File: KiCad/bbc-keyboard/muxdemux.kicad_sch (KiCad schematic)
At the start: 1 part, among them IC1 74LS161

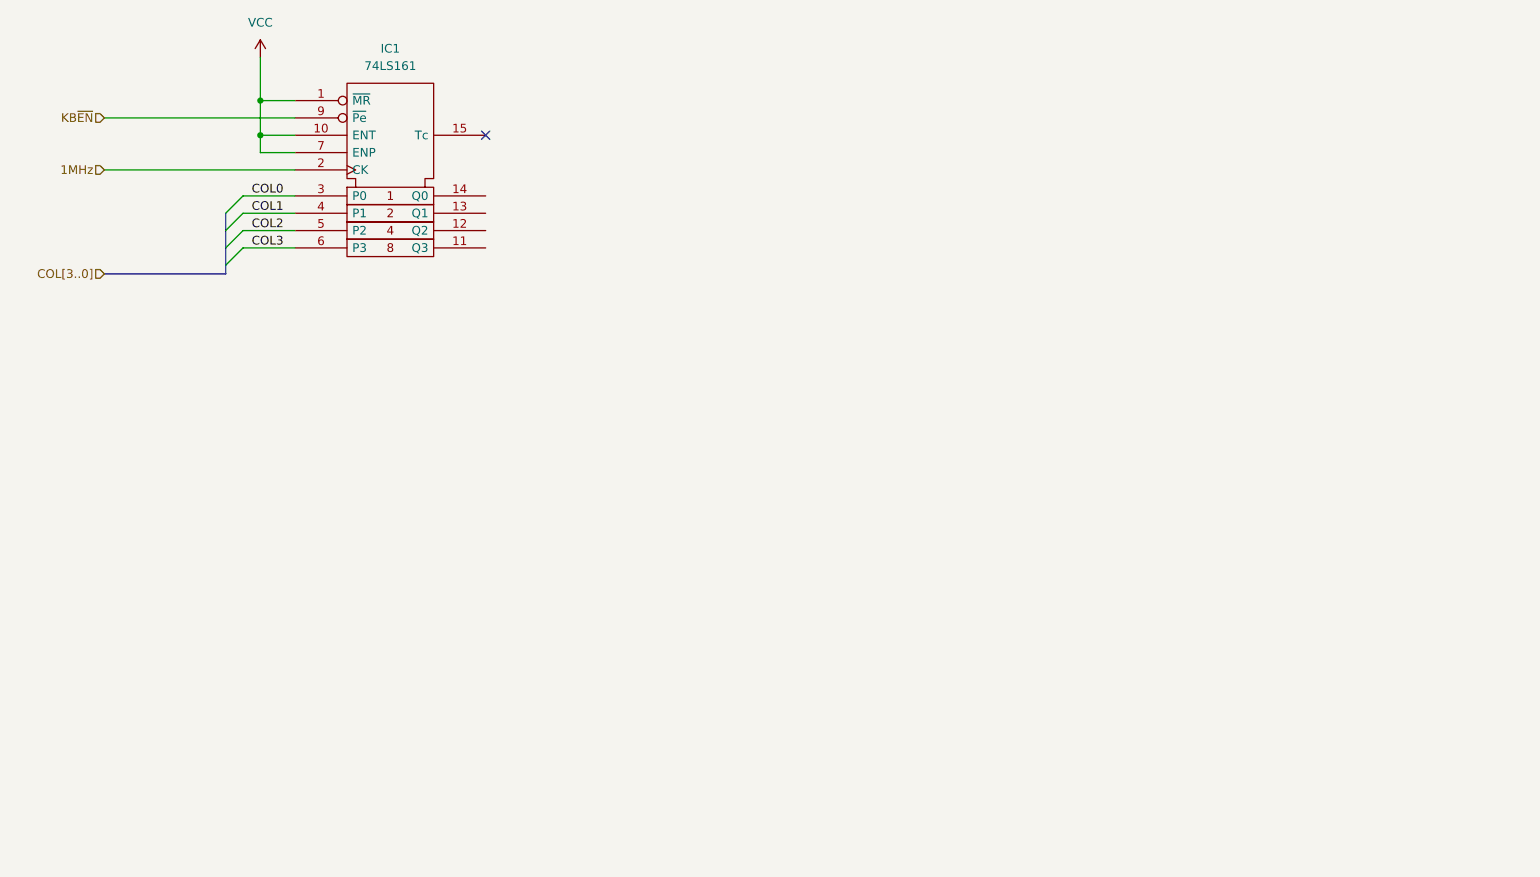
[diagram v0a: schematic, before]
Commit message: 1st cut mux/demux
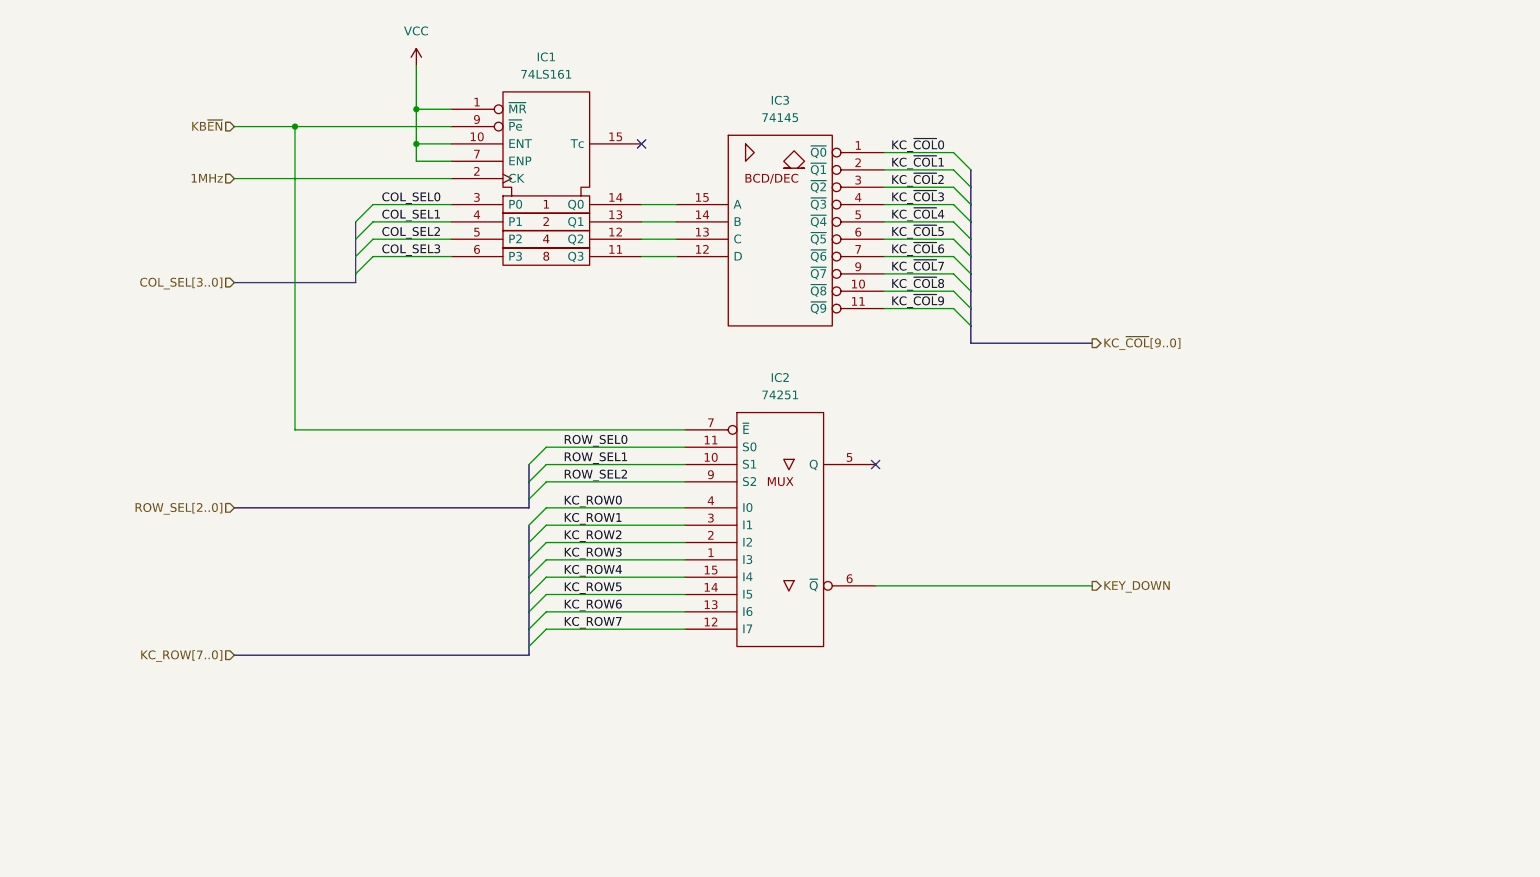
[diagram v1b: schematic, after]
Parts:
- added IC2: 74251, symbol 74xx_IEEE:74251
- added IC3: 74145, symbol 74xx_IEEE:74145
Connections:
- net GND: now also IC2.8 (GND), IC3.8 (GND)
- net KB~{EN}: now also IC2.7 (~{E})
- net VCC: now also IC2.16 (VCC), IC3.16 (VCC)
- net at IC1.11 (Q3): now also IC3.12 (D)
- net at IC1.12 (Q2): now also IC3.13 (C)
- net at IC1.13 (Q1): now also IC3.14 (B)
- net at IC1.14 (Q0): now also IC3.15 (A)
- net COL0 renamed COL_SEL0
- net COL1 renamed COL_SEL1
- net COL2 renamed COL_SEL2
- net COL3 renamed COL_SEL3
- new net KC_ROW0: IC2.4 (I0)
- new net KC_ROW1: IC2.3 (I1)
- new net KC_ROW2: IC2.2 (I2)
- new net KC_ROW3: IC2.1 (I3)
- new net KC_ROW4: IC2.15 (I4)
- new net KC_ROW5: IC2.14 (I5)
- new net KC_ROW6: IC2.13 (I6)
- new net KC_ROW7: IC2.12 (I7)
- new net KC_~{COL}0: IC3.1 (~{Q0})
- new net KC_~{COL}1: IC3.2 (~{Q1})
- new net KC_~{COL}2: IC3.3 (~{Q2})
- new net KC_~{COL}3: IC3.4 (~{Q3})
- new net KC_~{COL}4: IC3.5 (~{Q4})
- new net KC_~{COL}5: IC3.6 (~{Q5})
- new net KC_~{COL}6: IC3.7 (~{Q6})
- new net KC_~{COL}7: IC3.9 (~{Q7})
- new net KC_~{COL}8: IC3.10 (~{Q8})
- new net KC_~{COL}9: IC3.11 (~{Q9})
- new net KEY_DOWN: IC2.6 (~{Q})
- new net ROW_SEL0: IC2.11 (S0)
- new net ROW_SEL1: IC2.10 (S1)
- new net ROW_SEL2: IC2.9 (S2)
- no-connect marks 1 -> 2
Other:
- moved on the sheet: IC1

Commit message: muxdemux irq det
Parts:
- added IC4: 7430, symbol 74xx_IEEE:7430
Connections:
- net KC_ROW1: now also IC4.12
- net KC_ROW2: now also IC4.1
- net KC_ROW3: now also IC4.2
- net KC_ROW4: now also IC4.3
- net KC_ROW5: now also IC4.4
- net KC_ROW6: now also IC4.5
- net KC_ROW7: now also IC4.11
- net VCC: now also IC4.6
- new net Gnd: IC4.7 (Gnd)
- new net KEY_~{IRQ}: IC4.8
- new net Vcc: IC4.14 (Vcc)

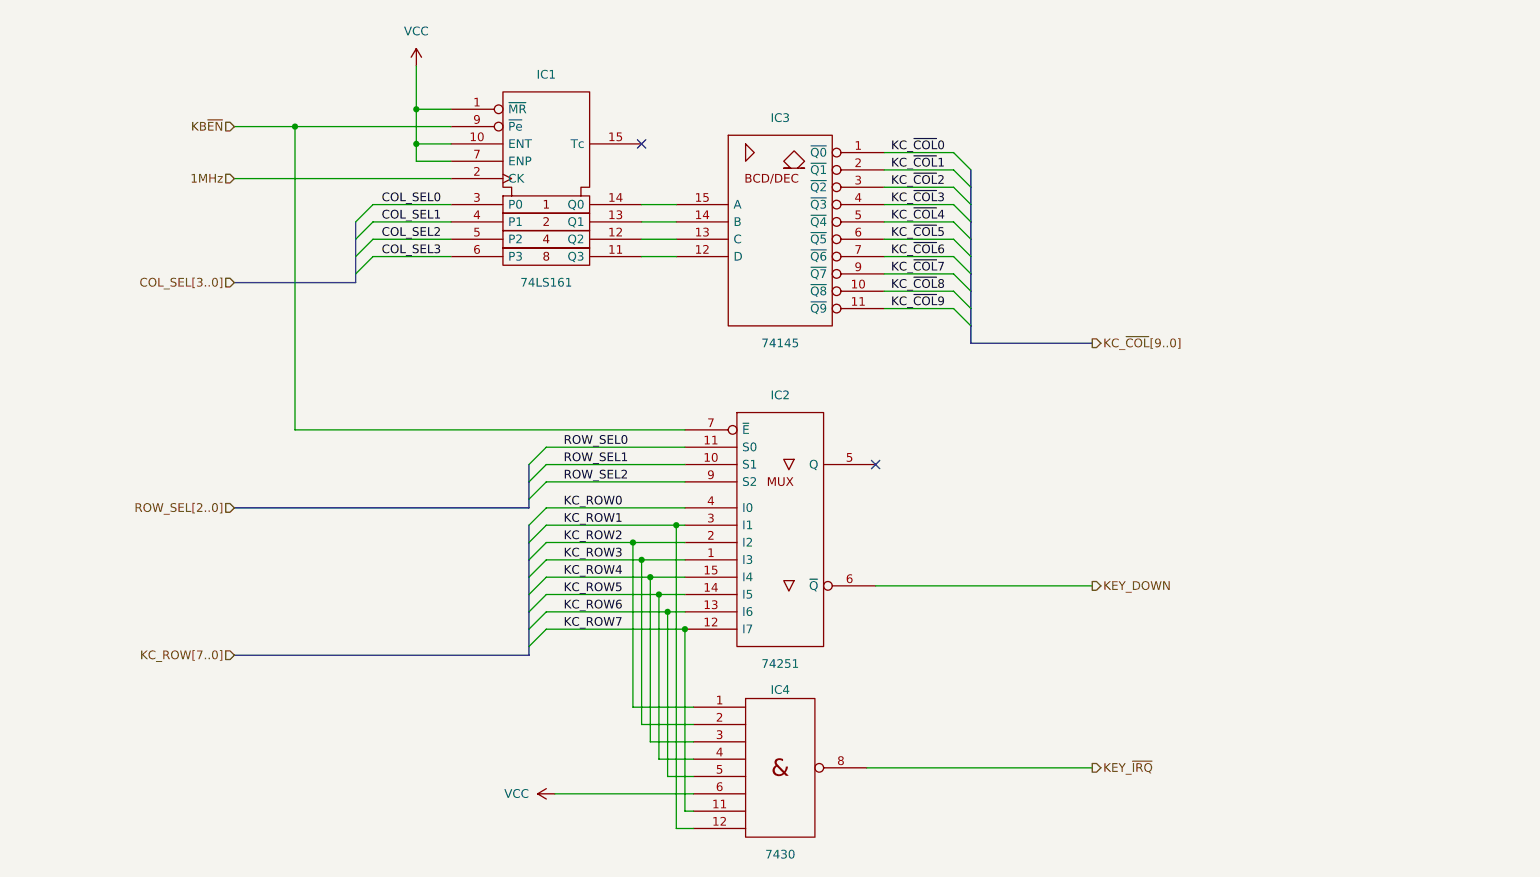
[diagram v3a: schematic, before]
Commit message: pull ups
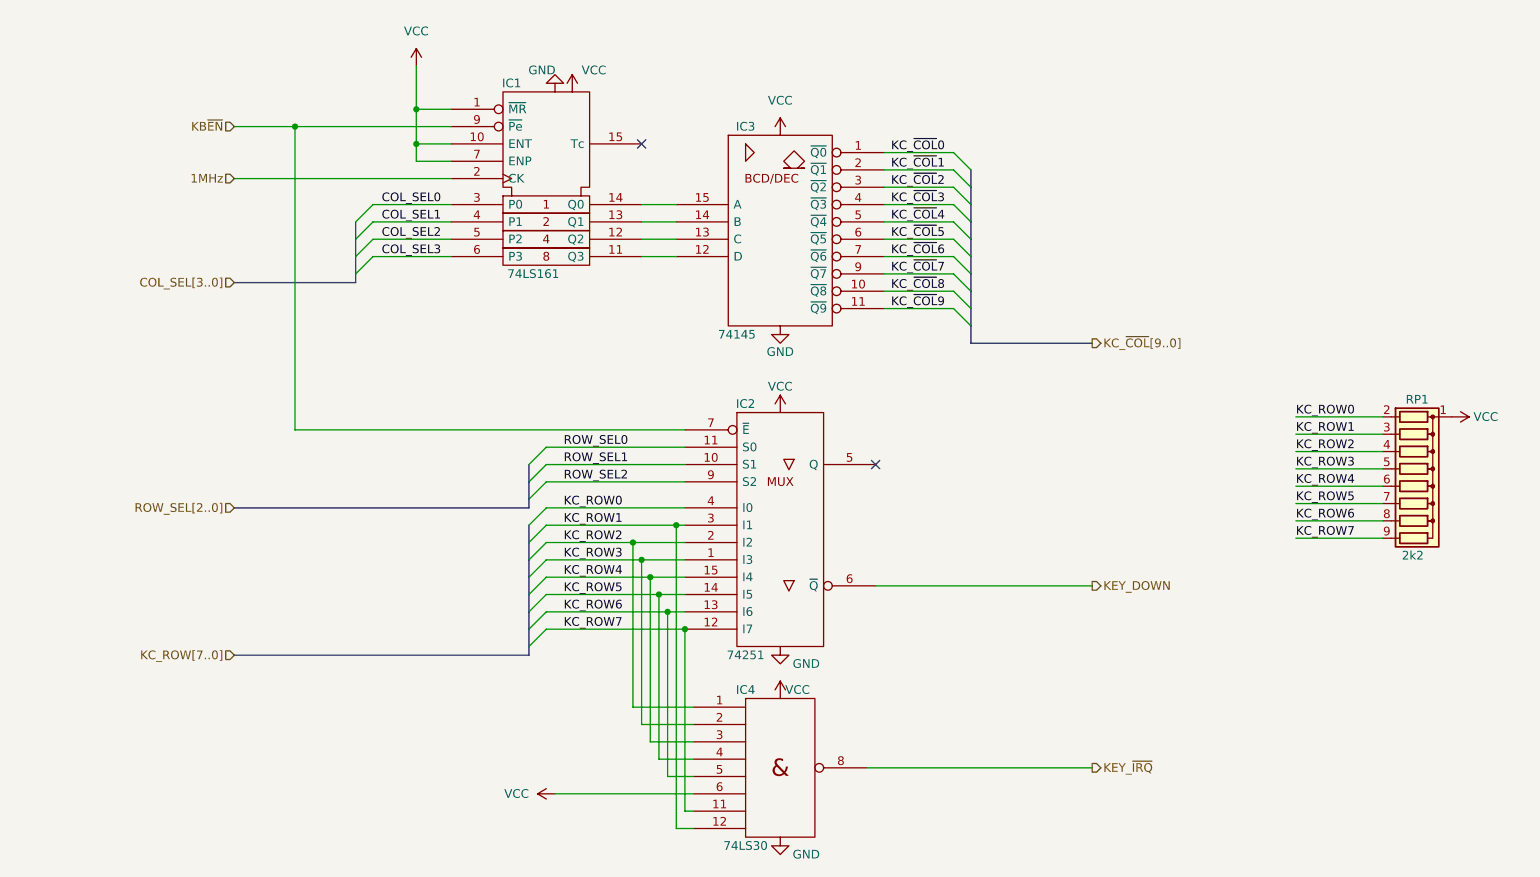
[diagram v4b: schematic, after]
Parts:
- added RP1: 2k2, Resistor_THT:R_Array_SIP9, symbol Device:R_Network08
- IC4: value 7430 -> 74LS30
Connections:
- net Gnd is gone; now on net GND: IC4.7 (Gnd)
- net Vcc is gone; now on net VCC: IC4.14 (Vcc)
- net KC_ROW0: now also RP1.2 (R1)
- net KC_ROW1: now also RP1.3 (R2)
- net KC_ROW2: now also RP1.4 (R3)
- net KC_ROW3: now also RP1.5 (R4)
- net KC_ROW4: now also RP1.6 (R5)
- net KC_ROW5: now also RP1.7 (R6)
- net KC_ROW6: now also RP1.8 (R7)
- net KC_ROW7: now also RP1.9 (R8)
- net VCC: now also RP1.1 (common)

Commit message: placing components
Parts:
- IC1, IC2, IC3: footprint (none) -> Package_DIP:DIP-16_W7.62mm
- IC4: footprint (none) -> Package_DIP:DIP-14_W7.62mm
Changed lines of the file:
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@@
     (property "Reference" "IC3" (id 0) (at 127 46.99 0))
     (property "Value" "74145" (id 1) (at 125.73 77.47 0))
-    (property "Footprint" "" (id 2) (at 132.08 62.23 0)
+    (property "Footprint" "Package_DIP:DIP-16_W7.62mm" (id 2) (at 132.08 62.23 0)
       (effects (font (size 1.27 1.27)) hide)
     )
@@
     (property "Reference" "IC1" (id 0) (at 92.71 40.64 0))
     (property "Value" "74LS161" (id 1) (at 95.885 68.58 0))
-    (property "Footprint" "" (id 2) (at 97.79 55.88 0)
+    (property "Footprint" "Package_DIP:DIP-16_W7.62mm" (id 2) (at 97.79 55.88 0)
       (effects (font (size 1.27 1.27)) hide)
     )
@@
     (property "Reference" "IC2" (id 0) (at 127 87.63 0))
     (property "Value" "74251" (id 1) (at 127 124.46 0))
-    (property "Footprint" "" (id 2) (at 132.08 105.41 0)
+    (property "Footprint" "Package_DIP:DIP-16_W7.62mm" (id 2) (at 132.08 105.41 0)
       (effects (font (size 1.27 1.27)) hide)
     )
@@
     (property "Reference" "IC4" (id 0) (at 127 129.54 0))
     (property "Value" "74LS30" (id 1) (at 127 152.4 0))
-    (property "Footprint" "" (id 2) (at 132.08 140.97 0)
+    (property "Footprint" "Package_DIP:DIP-14_W7.62mm" (id 2) (at 132.08 140.97 0)
       (effects (font (size 1.27 1.27)) hide)
     )

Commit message: routed rhs
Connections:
- net KC_ROW1: now also RP1.8 (R7); no longer RP1.3 (R2)
- net KC_ROW2: now also RP1.7 (R6); no longer RP1.4 (R3)
- net KC_ROW3: now also RP1.6 (R5); no longer RP1.5 (R4)
- net KC_ROW4: now also RP1.5 (R4); no longer RP1.6 (R5)
- net KC_ROW5: now also RP1.4 (R3); no longer RP1.7 (R6)
- net KC_ROW6: now also RP1.3 (R2); no longer RP1.8 (R7)
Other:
- moved on the sheet: RP1
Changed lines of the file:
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@@
     (stroke (width 0) (type default) (color 0 0 0 0))
   )
-  (wire (pts (xy 207.645 89.535) (xy 220.345 89.535))
+  (wire (pts (xy 210.82 128.27) (xy 223.52 128.27))
     (stroke (width 0) (type default) (color 0 0 0 0))
   )
@@
     (stroke (width 0) (type default) (color 0 0 0 0))
   )
-  (wire (pts (xy 207.645 107.315) (xy 220.345 107.315))
+  (wire (pts (xy 210.82 146.05) (xy 223.52 146.05))
     (stroke (width 0) (type default) (color 0 0 0 0))
   )
@@
     (stroke (width 0) (type default) (color 0 0 0 0))
   )
-  (wire (pts (xy 207.645 97.155) (xy 220.345 97.155))
+  (wire (pts (xy 210.82 135.89) (xy 223.52 135.89))
     (stroke (width 0) (type default) (color 0 0 0 0))
   )
@@
     (stroke (width 0) (type default) (color 0 0 0 0))
   )
-  (wire (pts (xy 207.645 102.235) (xy 220.345 102.235))
+  (wire (pts (xy 210.82 140.97) (xy 223.52 140.97))
     (stroke (width 0) (type default) (color 0 0 0 0))
   )
@@
     (stroke (width 0) (type default) (color 0 0 0 0))
   )
-  (wire (pts (xy 207.645 92.075) (xy 220.345 92.075))
+  (wire (pts (xy 210.82 130.81) (xy 223.52 130.81))
     (stroke (width 0) (type default) (color 0 0 0 0))
   )
@@
     (stroke (width 0) (type default) (color 0 0 0 0))
   )
-  (wire (pts (xy 207.645 94.615) (xy 220.345 94.615))
+  (wire (pts (xy 210.82 133.35) (xy 223.52 133.35))
     (stroke (width 0) (type default) (color 0 0 0 0))
   )
@@
     (stroke (width 0) (type default) (color 0 0 0 0))
   )
-  (wire (pts (xy 207.645 104.775) (xy 220.345 104.775))
+  (wire (pts (xy 210.82 143.51) (xy 223.52 143.51))
     (stroke (width 0) (type default) (color 0 0 0 0))
   )
@@
     (stroke (width 0) (type default) (color 0 0 0 0))
   )
-  (wire (pts (xy 207.645 99.695) (xy 220.345 99.695))
+  (wire (pts (xy 210.82 138.43) (xy 223.52 138.43))
     (stroke (width 0) (type default) (color 0 0 0 0))
   )
@@
     (effects (font (size 1.27 1.27)) (justify right bottom))
   )
-  (label "KC_ROW6" (at 207.645 104.775 0)
+  (label "KC_ROW6" (at 210.82 130.81 0)
     (effects (font (size 1.27 1.27)) (justify left bottom))
   )
@@
     (effects (font (size 1.27 1.27)) (justify left bottom))
   )
-  (label "KC_ROW3" (at 207.645 97.155 0)
+  (label "KC_ROW3" (at 210.82 138.43 0)
     (effects (font (size 1.27 1.27)) (justify left bottom))
   )
@@
     (effects (font (size 1.27 1.27)) (justify left bottom))
   )
-  (label "KC_ROW0" (at 207.645 89.535 0)
+  (label "KC_ROW0" (at 210.82 128.27 0)
     (effects (font (size 1.27 1.27)) (justify left bottom))
   )
@@
     (effects (font (size 1.27 1.27)) (justify left bottom))
   )
-  (label "KC_ROW1" (at 207.645 92.075 0)
+  (label "KC_ROW1" (at 210.82 143.51 0)
     (effects (font (size 1.27 1.27)) (justify left bottom))
   )
@@
     (effects (font (size 1.27 1.27)) (justify right bottom))
   )
-  (label "KC_ROW7" (at 207.645 107.315 0)
+  (label "KC_ROW7" (at 210.82 146.05 0)
     (effects (font (size 1.27 1.27)) (justify left bottom))
   )
@@
     (effects (font (size 1.27 1.27)) (justify right bottom))
   )
-  (label "KC_ROW4" (at 207.645 99.695 0)
+  (label "KC_ROW4" (at 210.82 135.89 0)
     (effects (font (size 1.27 1.27)) (justify left bottom))
   )
@@
     (effects (font (size 1.27 1.27)) (justify left bottom))
   )
-  (label "KC_ROW2" (at 207.645 94.615 0)
+  (label "KC_ROW2" (at 210.82 140.97 0)
     (effects (font (size 1.27 1.27)) (justify left bottom))
   )
@@
     (effects (font (size 1.27 1.27)) (justify left bottom))
   )
-  (label "KC_ROW5" (at 207.645 102.235 0)
+  (label "KC_ROW5" (at 210.82 133.35 0)
     (effects (font (size 1.27 1.27)) (justify left bottom))
   )
@@
     (pin "1")
   )
-  (symbol (lib_id "power:VCC") (at 230.505 89.535 270) (unit 1)
+  (symbol (lib_id "power:VCC") (at 233.68 128.27 270) (unit 1)
     (in_bom yes) (on_board yes) (fields_autoplaced)
-    (property "Reference" "#PWR0109" (id 0) (at 226.695 89.535 0)
-      (effects (font (size 1.27 1.27)) hide)
-    )
-    (property "Value" "VCC" (id 1) (at 233.68 89.5349 90)
+    (property "Reference" "#PWR0109" (id 0) (at 229.87 128.27 0)
+      (effects (font (size 1.27 1.27)) hide)
+    )
+    (property "Value" "VCC" (id 1) (at 236.855 128.2699 90)
       (effects (font (size 1.27 1.27)) (justify left))
     )
-    (property "Footprint" "" (id 2) (at 230.505 89.535 0)
-      (effects (font (size 1.27 1.27)) hide)
-    )
-    (property "Datasheet" "" (id 3) (at 230.505 89.535 0)
+    (property "Footprint" "" (id 2) (at 233.68 128.27 0)
+      (effects (font (size 1.27 1.27)) hide)
+    )
+    (property "Datasheet" "" (id 3) (at 233.68 128.27 0)
       (effects (font (size 1.27 1.27)) hide)
     )
@@
     (pin "1")
   )
-  (symbol (lib_id "Device:R_Network08") (at 225.425 99.695 270) (unit 1)
-    (in_bom yes) (on_board yes)
-    (property "Reference" "RP1" (id 0) (at 225.425 86.995 90))
-    (property "Value" "2k2" (id 1) (at 224.79 109.855 90))
-    (property "Footprint" "Resistor_THT:R_Array_SIP9" (id 2) (at 225.425 111.76 90)
-      (effects (font (size 1.27 1.27)) hide)
-    )
-    (property "Datasheet" "http://www.vishay.com/docs/31509/csc.pdf" (id 3) (at 225.425 99.695 0)
-      (effects (font (size 1.27 1.27)) hide)
-    )
+  (symbol (lib_id "Device:R_Network08") (at 228.6 138.43 270) (unit 1)
+    (in_bom yes) (on_board yes)
+    (property "Reference" "RP1" (id 0) (at 228.6 125.73 90))
+    (property "Value" "2k2" (id 1) (at 227.965 148.59 90))
+    (property "Footprint" "Resistor_THT:R_Array_SIP9" (id 2) (at 228.6 150.495 90)
+      (effects (font (size 1.27 1.27)) hide)
+    )
+    (property "Datasheet" "http://www.vishay.com/docs/31509/csc.pdf" (id 3) (at 228.6 138.43 0)
+      (effects (font (size 1.27 1.27)) hide)
+    )
